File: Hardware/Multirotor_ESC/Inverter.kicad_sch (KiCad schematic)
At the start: 1 part

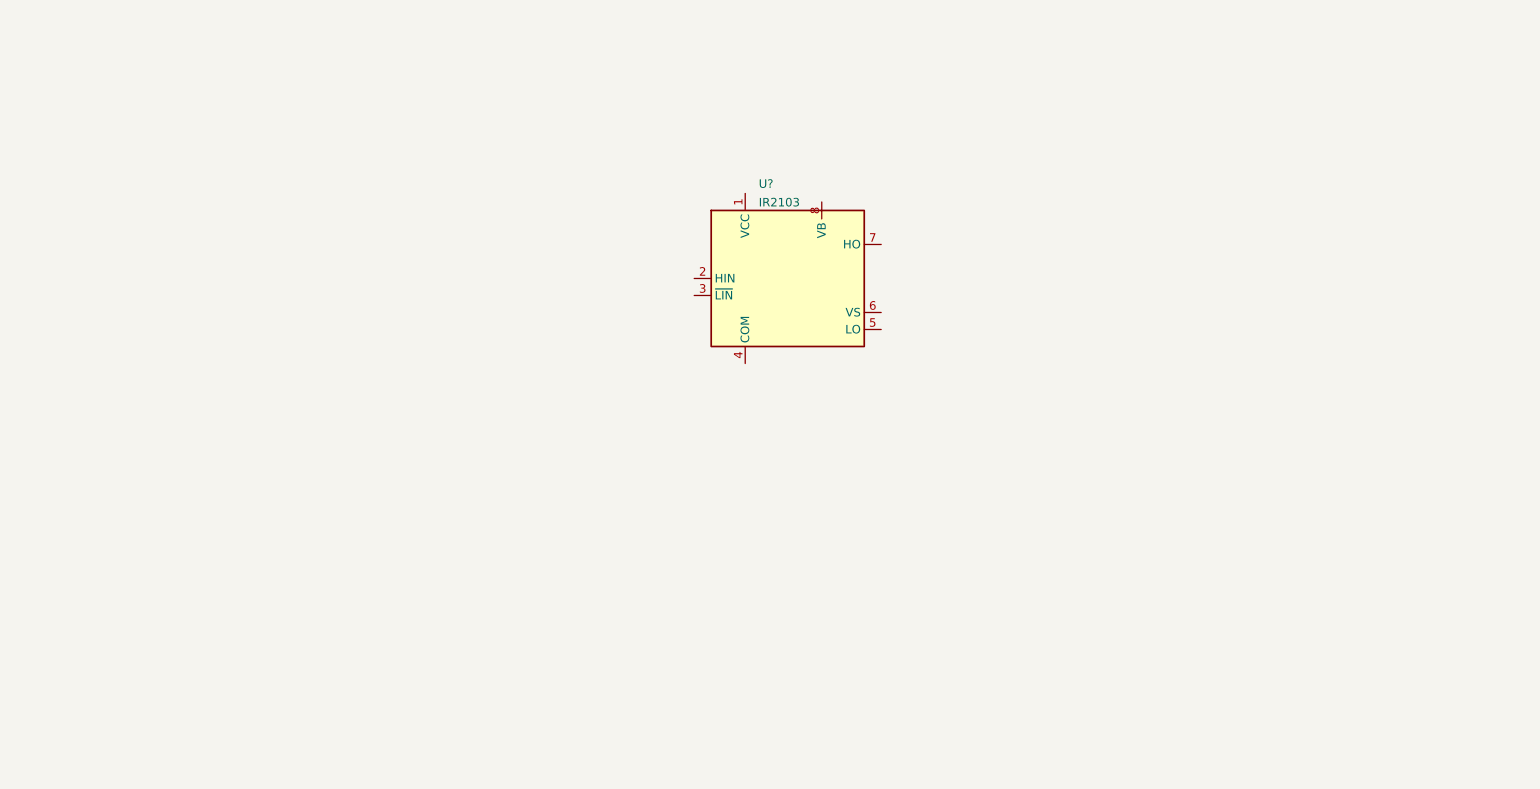
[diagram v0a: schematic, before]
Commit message: Added Phase Half-Bridge Circuit
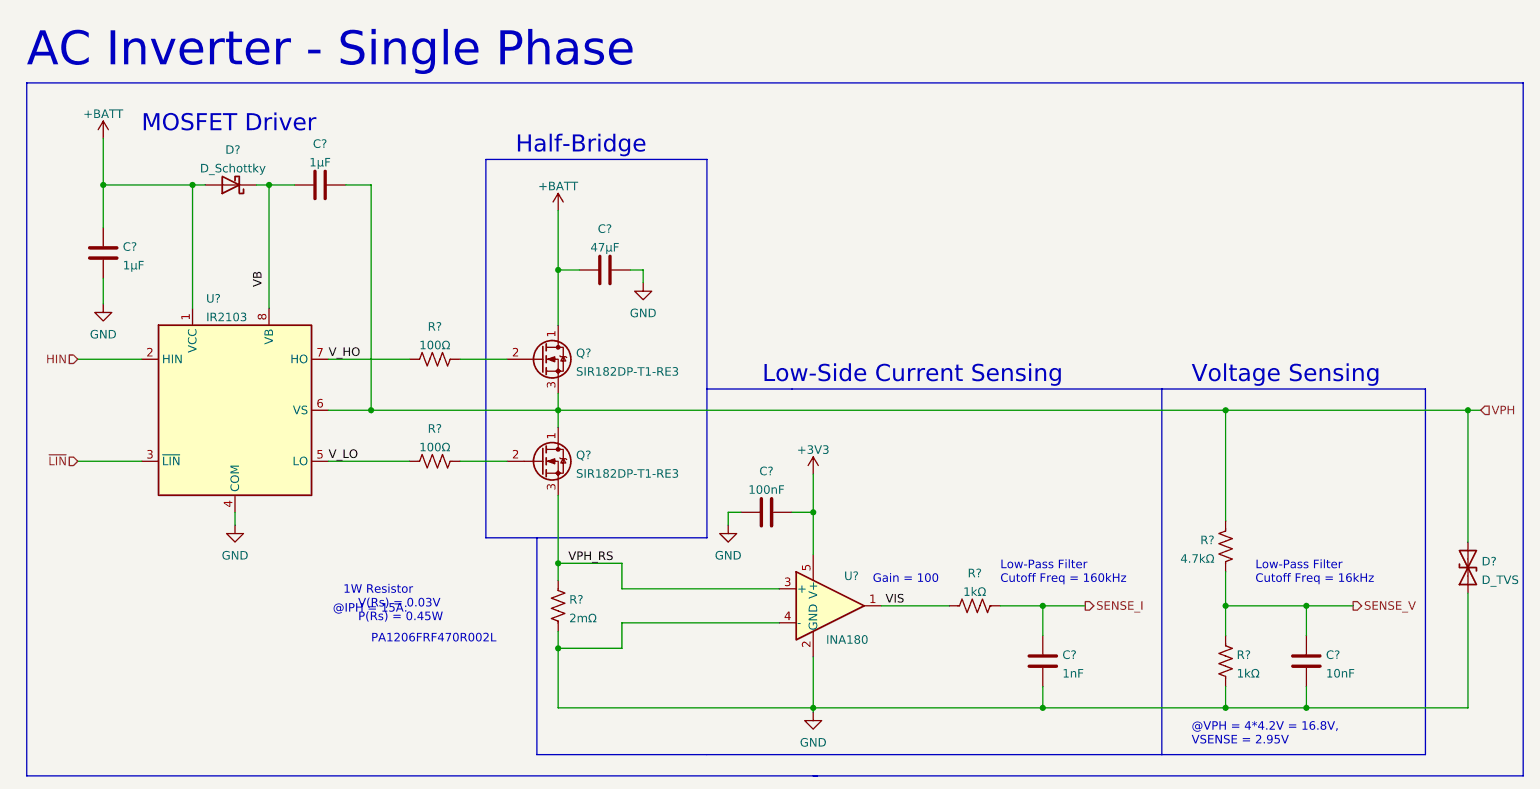
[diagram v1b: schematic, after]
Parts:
- added C?: 47μF, symbol Device:C
- added C? (x2): 1μF, symbol Device:C
- added C?: 1nF, symbol Device:C
- added C?: 100nF, symbol Device:C
- added C?: 10nF, symbol Device:C
- added D?: D_TVS, symbol Device:D_TVS
- added D?: D_Schottky, symbol Device:D_Schottky
- added Q? (x2): SIR182DP-T1-RE3, symbol Transistor_FET:IRL6283M
- added R?: 4.7kΩ, symbol Device:R_US
- added R? (x2): 100Ω, symbol Device:R_US
- added R?: 2mΩ, symbol Device:R_US
- added R? (x2): 1kΩ, symbol Device:R_US
- added U?: INA180, Package_TO_SOT_SMD:SOT-23-5, symbol Amplifier_Current:INA169
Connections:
- net +BATT: now reaches U?.1 (VCC)
- net +BATT: now also C?.1, C?.2, D?.2 (A), Q?.1 (D)
- net HIN: now reaches U?.2 (HIN)
- net ~{LIN}: now reaches U?.3 (~{LIN})
- net GND: now reaches U?.4 (COM)
- net GND: now also C?.1, C?.1, C?.1, C?.1, C?.2, D?.1 (A1), R?.1, R?.2, U?.2 (GND), U?.4 (-)
- net V_LO: now reaches U?.5 (LO)
- net V_LO: now also R?.1
- net VPH: now reaches U?.6 (VS)
- net VPH: now also C?.2, D?.2 (A2), Q?.1 (D), Q?.3 (S), R?.2
- net V_HO: now reaches U?.7 (HO)
- net V_HO: now also R?.1
- net at U?.8 (VB): now also C?.1, D?.1 (K)
- new net: Q?.2 (G), R?.2 (x2)
- new net +3V3: C?.2, U?.5 (V+)
- new net SENSE_I: C?.2, R?.1
- new net SENSE_V: C?.2, R?.1, R?.1
- new net VIS: R?.2, U?.1
- new net VPH_RS: Q?.3 (S), R?.2, U?.3 (+)
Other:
- note added: "1W Resistor V(Rs) = 0.03V P(Rs) = 0.45W"
- note added: "@IPH = 15A:"
- note added: "@VPH = 4*4.2V = 16.8V, VSENSE = 2.95V"
- note added: "AC Inverter - Single Phase"
- note added: "Gain = 100"
- note added: "Half-Bridge"
- note added: "Low-Pass Filter Cutoff Freq = 160kHz"
- note added: "Low-Pass Filter Cutoff Freq = 16kHz"
- note added: "Low-Side Current Sensing"
- note added: "MOSFET Driver"
- note added: "PA1206FRF470R002L"
- note added: "Voltage Sensing"
- moved on the sheet: U?
